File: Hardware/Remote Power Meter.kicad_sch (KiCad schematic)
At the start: 30 parts, among them J1 USB_C_Receptacle_USB2.0, J2 Conn_01x04_Female, J3 Conn_01x04_Male, J4 Conn_01x02, J5 USB_A, J6 Conn_01x02, SW1 SW_Push, U1 AMS1117-3.3, U2 INA219AxD, U3 CH340C

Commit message: Now programmable via USB
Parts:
- added Q1: UMH3N, Package_TO_SOT_SMD:SOT-363_SC-70-6, symbol Transistor_BJT:UMH3N
- added R13, R14: 10K, Resistor_SMD:R_0603_1608Metric, symbol Device:R
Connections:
- net 3v3: now also R13.2
- net DTR: now also Q1.2 (B1), Q1.3 (C2)
- net RST: now also Q1.6 (C1)
- net RTS: now also Q1.1 (E1), Q1.5 (B2)
- net TxD: now also R13.1
- net IO16: now reaches Um1.1 (GPIO16)
- net IO2: now reaches Um1.10 (GPIO2)
- net IO0: now reaches Um1.11 (GPIO0)
- net IO0: now also Q1.4 (E2), R14.1
- net IO13: now reaches Um1.3 (GPIO13)
- new net +3V3: R14.2
- no-connect marks 17 -> 14
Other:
- note added: "Programming"
- note added: "USB Communication"
- note removed: "ESP Programmer"
- note removed: "Programmer"
- moved on the sheet: C1, C2, C3, C4, C5, J2, J3, J4, J5, J6, JP1, JP2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

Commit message: Possibly reached v1.0.0
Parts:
- added C6, C7: 0.1, Capacitor_SMD:C_0603_1608Metric_Pad1.08x0.95mm_HandSolder, symbol Device:C
- added D1, D2: WS2812B, LED_SMD:LED_WS2812B_PLCC4_5.0x5.0mm_P3.2mm, symbol LED:WS2812B
- added J7: Conn_01x04_Male, Connector_PinHeader_2.54mm:PinHeader_1x04_P2.54mm_Vertical, symbol Connector:Conn_01x04_Male
- added R15: 470, Resistor_SMD:R_0603_1608Metric_Pad0.98x0.95mm_HandSolder, symbol Device:R
- added USB1: 48037-0001, Tinker:USB-A-TH_48037-0001, symbol USB-A-TH_48037-0001:48037-0001
- J3: footprint Connector_PinHeader_2.54mm:PinHeader_1x04_P2.54mm_Horizontal -> Connector_PinHeader_2.54mm:PinHeader_1x04_P2.54mm_Vertical
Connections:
- net 3v3: now also C6.1, C7.1, D1.1 (VDD), D2.1 (VDD)
- net D+: now also J7.3 (Pin_3), USB1.3 (D+)
- net D-: now also J7.2 (Pin_2), USB1.2 (D-)
- net GND: now also C6.2, C7.2, D1.3 (VSS), D2.3 (VSS), J7.4 (Pin_4), USB1.4 (GND), USB1.5 (EH), USB1.6 (EH)
- net IO13: now also R15.1
- net Vload: now also J7.1 (Pin_1)
- net Vsource: now also USB1.1 (VCC)
- new net: D1.2 (DOUT), D2.4 (DIN)
- new net: D1.4 (DIN), R15.2
- no-connect marks 14 -> 13
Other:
- note added: "Status LEDs"
- moved on the sheet: C2, C3, J2, J3, J4, J6, JP1, JP2, R12, R3, R4, R5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

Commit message: ...
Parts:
- added JP3: vLED, Jumper:SolderJumper-3_P1.3mm_Bridged12_RoundedPad1.0x1.5mm, symbol Jumper:SolderJumper_3_Bridged12
- added R16: 10K, Resistor_SMD:R_0603_1608Metric_Pad0.98x0.95mm_HandSolder, symbol Device:R
- added R2: 0.1, Resistor_SMD:R_2816_7142Metric_Pad3.20x4.45mm_HandSolder, symbol Device:R
- R1: renamed from R3; LCSC (none) -> C844084
- Um1: symbol Tinker-ESP:ESP-M3 -> esp-m3:ESP-M3
- renumbered J2 to Disp1, USB1 to J2, R4 to R10, R10 to R12, R12 to R17, R6 to R3, R7 to R4, R9 to R5, R8 to R6, R1 to R7, R2 to R8, R5 to R9
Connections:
- net 3v3: now also JP3.1 (A), R16.1; no longer C6.1, C7.1, D1.1 (VDD), D2.1 (VDD)
- net IO0: now also R15.1
- net IO13: no longer R15.1
- net Vcc: now also JP3.3 (B)
- net Vload: now also R2.1
- net Vsource: now also R2.2
- net EN: now reaches Um1.4 (EN)
- net EN: now also R16.2
- new net: C6.1, C7.1, D1.1 (VDD), D2.1 (VDD), JP3.2 (C)
- no-connect marks 13 -> 12
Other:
- note added: "Option: dual shunt resistors for higher current handling. (& possibly better accuracy.)"
- moved on the sheet: C2, C3, C7, D2, Disp1, R1, R10, R15, R17, R3, R4, R9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

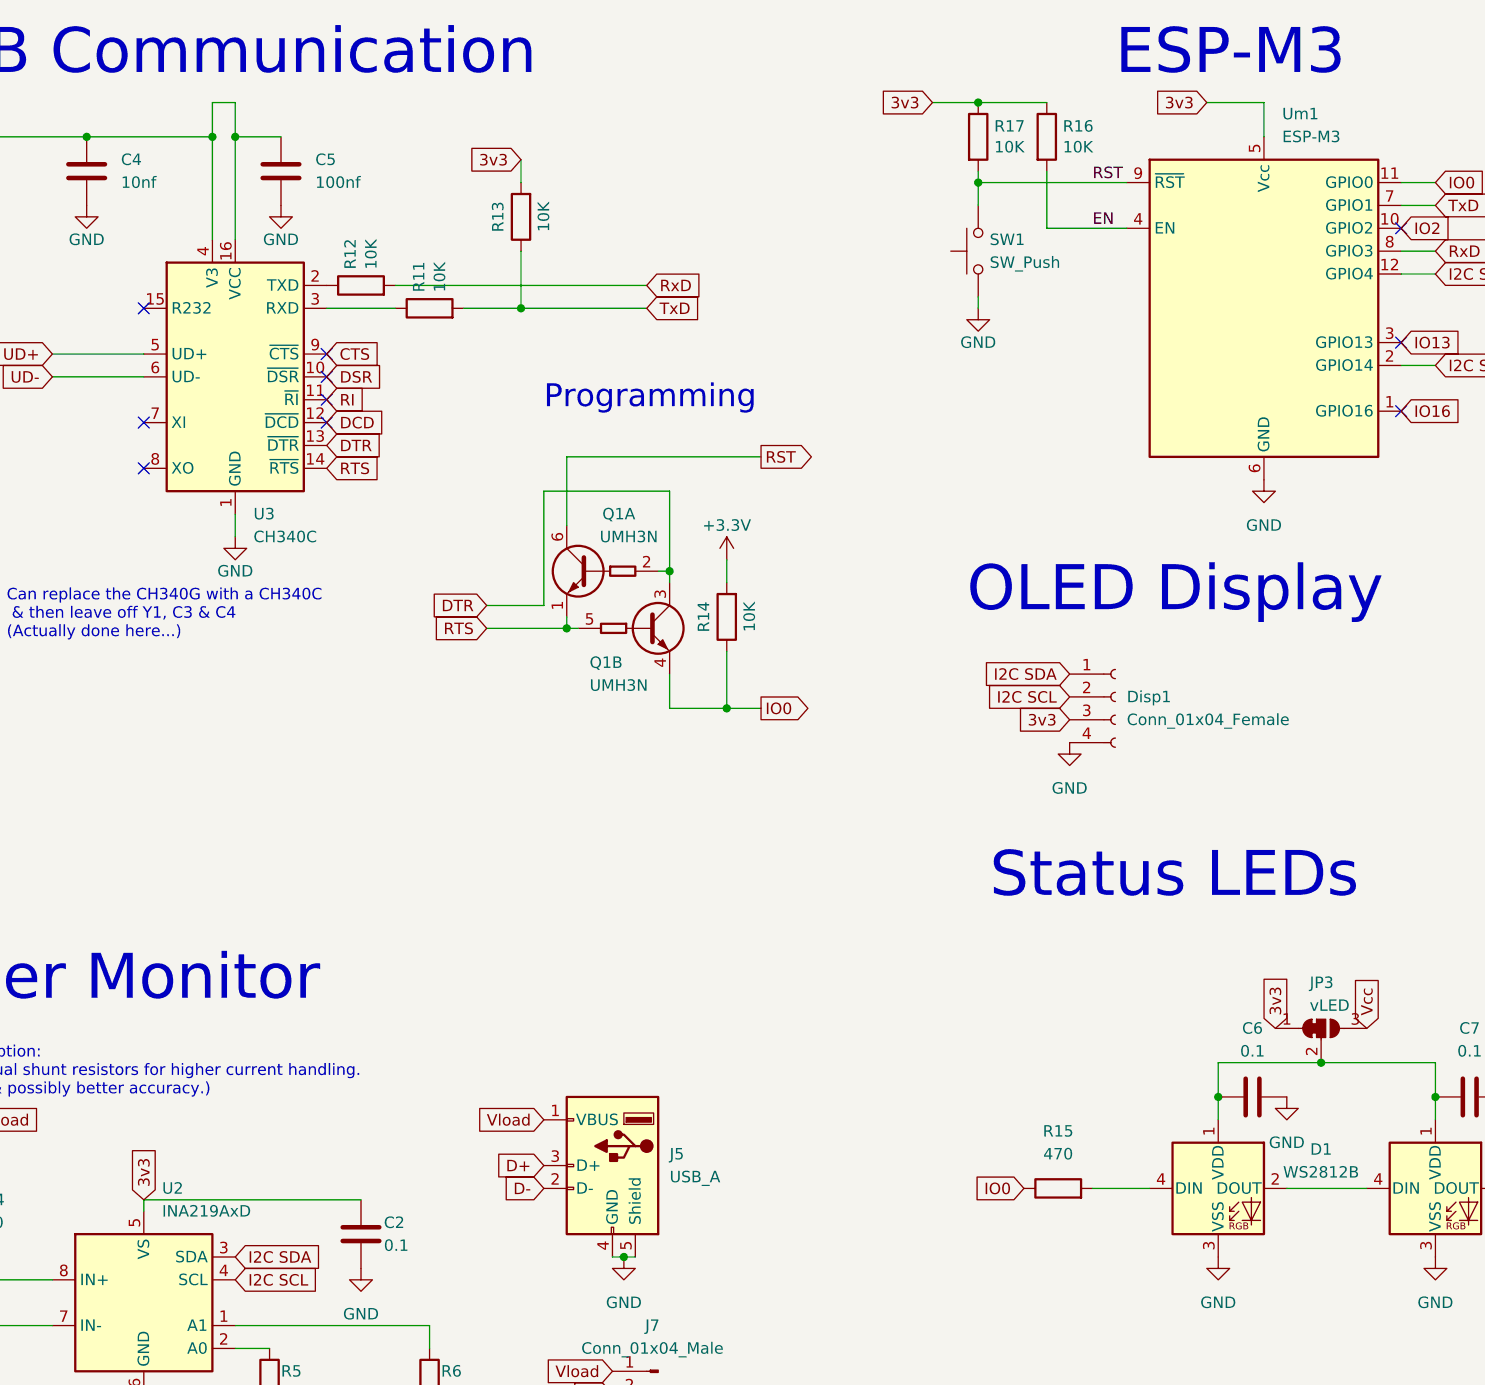
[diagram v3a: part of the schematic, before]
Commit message: Added LCSC BOM
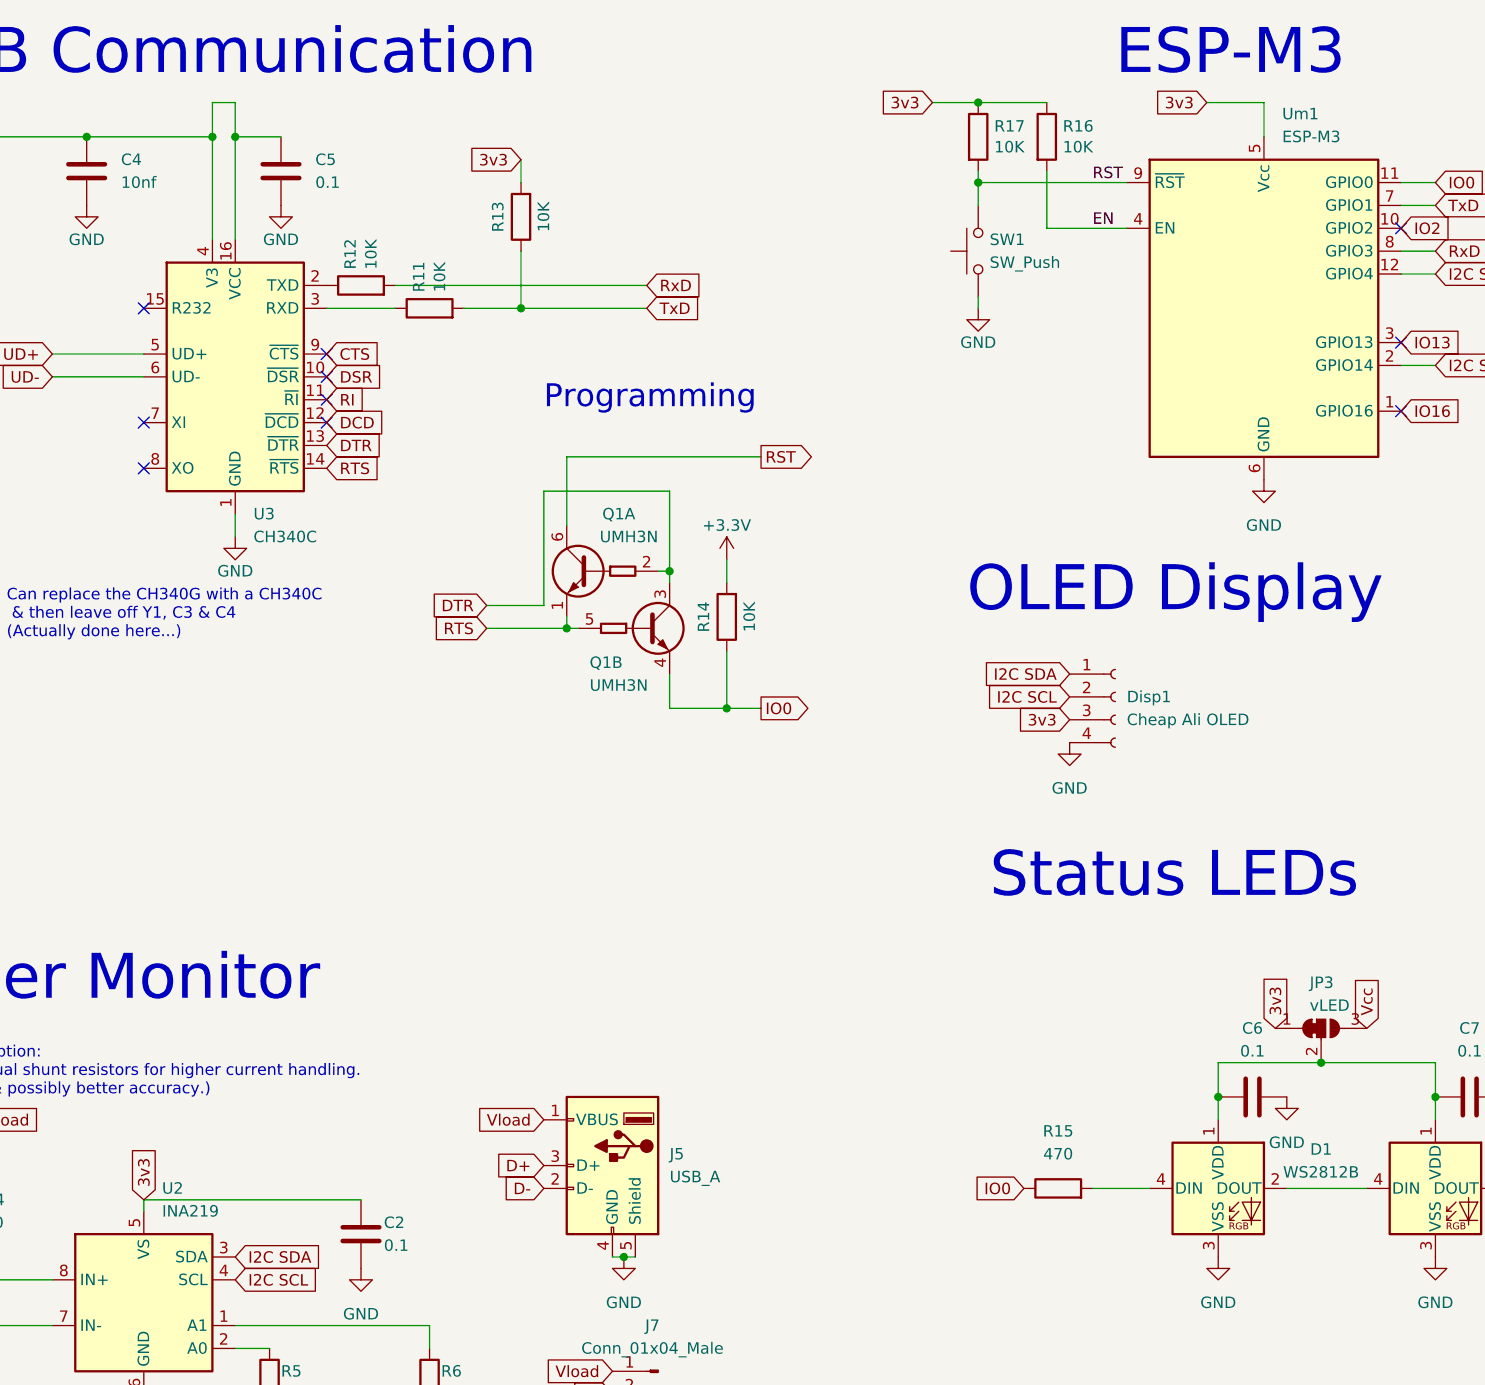
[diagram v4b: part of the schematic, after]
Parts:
- C1: LCSC (none) -> C145122
- C2, C3, C6, C7: LCSC (none) -> C14663
- C5: value 100nf -> 0.1; LCSC C235731 -> C14663
- D1, D2: LCSC (none) -> C2843785
- Disp1: value Conn_01x04_Female -> Cheap Ali OLED
- J1: LCSC (none) -> C2765186
- J2: LCSC (none) -> C136455; LCSC Part C136455 -> (none)
- J4, J6: LCSC (none) -> C784940
- J5: LCSC (none) -> C6389922
- JP1, JP2, JP3: now left out of the parts list
- R13, R14: footprint Resistor_SMD:R_0603_1608Metric -> Resistor_SMD:R_0603_1608Metric_Pad0.98x0.95mm_HandSolder
- R15: LCSC (none) -> C114669
- R3, R4: LCSC (none) -> C22859
- R7, R8: LCSC (none) -> C23203
- U1: LCSC (none) -> C347256
- U2: value INA219AxD -> INA219; LCSC (none) -> C138706
- Um1: LCSC (none) -> C19949058
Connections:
- net 3v3: now also C5.2; no longer C5.1
- net GND: now also C5.1; no longer C5.2
